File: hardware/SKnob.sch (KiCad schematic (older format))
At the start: 68 parts, among them J1 USB_B_Micro, J2 Conn_01x02, J3 Conn_01x02, SW1 SW_Push, T1 LA_LOGO, T2 LA_LOGO, U1 STM32WB55Cx, U2 LIS2DE12TR, U3 USBLC6-2P6, Y1 32MHz, Y2 32.768kHz

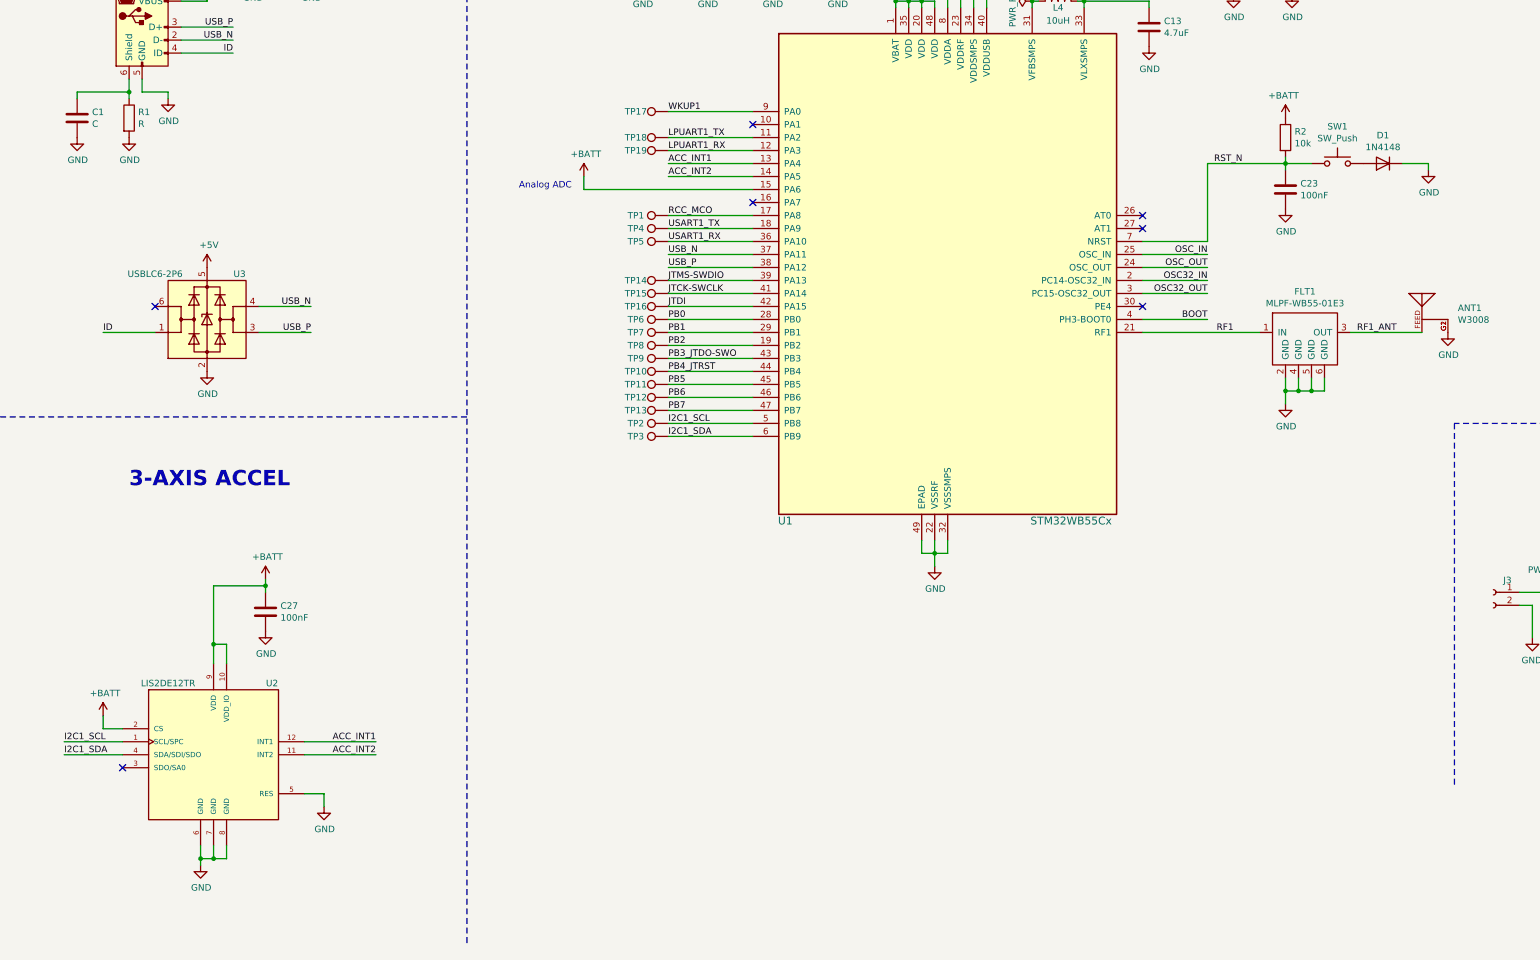
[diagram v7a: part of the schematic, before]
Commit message: added buzzer to PE4
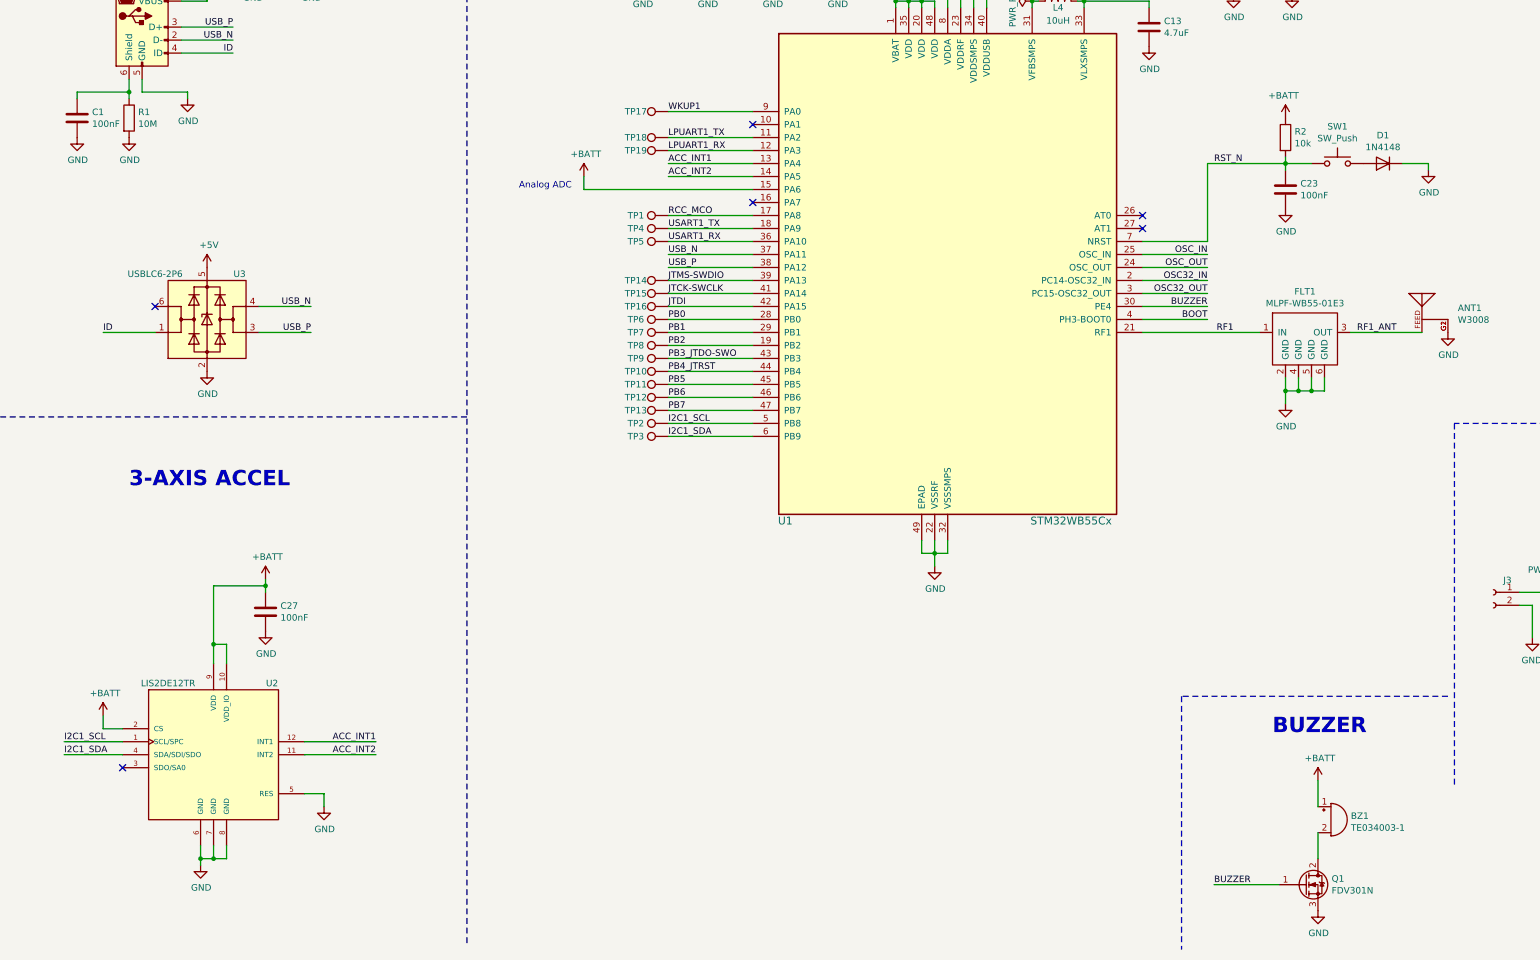
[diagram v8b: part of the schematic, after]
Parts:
- added BZ1: TE034003-1, SKnob:TE034003-1, symbol Device:Buzzer
- added Q1: FDV301N, Package_TO_SOT_SMD:SOT-23, symbol Device:Q_NMOS_GDS
- ANT1: Info 2.4GHz Bluetooth Chip RF Antenna 2.4GHz ~ 2.483GHz 1.7dBi S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 -> (none); info (none) -> 2.4GHz Bluetooth Chip RF Antenna 2.4GHz ~ 2.483GHz 1.7dBi S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
- BT1: Info Battery Retainer Coin, 12.0mm 1 Cell SMD (SMT) Tab -> (none); info (none) -> Battery Retainer Coin, 12.0mm 1 Cell SMD (SMT) Tab
- C1: value C -> 100nF
- D1: Info Diode Standard 100V 150mA Surface Mount DFN1006-2 -> (none); info (none) -> Diode Standard 100V 150mA Surface Mount DFN1006-2
- FLT1: Info 2.45GHz Center Frequency Low Pass RF Filter (Radio Frequenc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 -> (none); info (none) -> 2.45GHz Center Frequency Low Pass RF Filter (Radio Frequenc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
- L4: Info 10µH Unshielded Wirewound Inductor 380mA 468mOhm Max 0603 (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 -> (none); info (none) -> 10µH Unshielded Wirewound Inductor 380mA 468mOhm Max 0603 (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
- R1: value R -> 10M
- U1: Info IC RF TxRx + MCU 802.15.4, Bluetooth Bluetooth v5.0 2.405GH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 -> (none); info (none) -> IC RF TxRx + MCU 802.15.4, Bluetooth Bluetooth v5.0 2.405GH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
- U2: Info Accelerometer X, Y, Z Axis ±2g, 4g, 8g, 16g 0.5Hz ~ 2.69kHz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 -> (none); info (none) -> Accelerometer X, Y, Z Axis ±2g, 4g, 8g, 16g 0.5Hz ~ 2.69kHz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
- U3: Info 17V Clamp 5A (8/20µs) Ipp Tvs Diode Surface Mount SOT-666 -> (none); info (none) -> 17V Clamp 5A (8/20µs) Ipp Tvs Diode Surface Mount SOT-666
- Y1: Info 32MHz ±10ppm Crystal 10pF 60 Ohms 4-SMD, No Lead -> (none); info (none) -> 32MHz ±10ppm Crystal 10pF 60 Ohms 4-SMD, No Lead
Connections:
- net +BATT: now also BZ1.1 (-)
- net GND: now also Q1.3 (S)
- net BUZZER: now reaches U1.30 (PE4)
- net BUZZER: now also Q1.1 (G)
- new net: BZ1.2 (+), Q1.2 (D)
- no-connect marks 7 -> 6
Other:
- note added: "BUZZER"
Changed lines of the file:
@@
 F 2 "Battery:BatteryHolder_Keystone_3000_1x12mm" V 14800 8760 50  0001 C CNN
 F 3 "https://www.memoryprotectiondevices.com/datasheets/BK-885-datasheet.pdf" V 14800 8760 50  0001 C CNN
-F 4 "Battery Retainer Coin, 12.0mm 1 Cell SMD (SMT) Tab" H 14918 8659 50  0001 L CNN "Info"
-F 5 "MPD (Memory Protection Devices)" H 14800 8700 50  0001 C CNN "manf"
-F 6 "BK-885-TR" H 14800 8700 50  0001 C CNN "manf#"
-F 7 "BK-885-CT-ND" H 14800 8700 50  0001 C CNN "digikey#"
+F 4 "MPD (Memory Protection Devices)" H 14800 8700 50  0001 C CNN "manf"
+F 5 "BK-885-TR" H 14800 8700 50  0001 C CNN "manf#"
+F 6 "BK-885-CT-ND" H 14800 8700 50  0001 C CNN "digikey#"
+F 7 "Battery Retainer Coin, 12.0mm 1 Cell SMD (SMT) Tab" H 14800 8700 50  0001 C CNN "info"
 	1    14800 8700
 	1    0    0    -1
@@
 F 5 "W3008" H 11550 6350 50  0001 C CNN "manf#"
 F 6 "PulseLarsen Antennas" H 11550 6350 50  0001 C CNN "manf"
-F 7 "2.4GHz Bluetooth Chip RF Antenna 2.4GHz ~ 2.483GHz 1.7dBi Solder Surface Mount" H 11550 6350 50  0001 C CNN "Info"
+F 7 "2.4GHz Bluetooth Chip RF Antenna 2.4GHz ~ 2.483GHz 1.7dBi Solder Surface Mount" H 11550 6350 50  0001 C CNN "info"
 	1    11550 6350
 	1    0    0    -1
@@
 F 5 "STMicroelectronics" H 6400 4750 50  0001 C CNN "manf"
 F 6 "STM32WB55CGU6" H 6400 4750 50  0001 C CNN "manf#"
-F 7 "IC RF TxRx + MCU 802.15.4, Bluetooth Bluetooth v5.0 2.405GHz ~ 2.48GHz 48-UFQFN Exposed Pad" H 6400 4750 50  0001 C CNN "Info"
+F 7 "IC RF TxRx + MCU 802.15.4, Bluetooth Bluetooth v5.0 2.405GHz ~ 2.48GHz 48-UFQFN Exposed Pad" H 6400 4750 50  0001 C CNN "info"
 	1    6400 4750
 	1    0    0    -1
@@
 F 5 "CBMF1608T100K" V 8750 3900 50  0001 C CNN "manf#"
 F 6 "587-1720-1-ND" V 8750 3900 50  0001 C CNN "digikey#"
-F 7 "10µH Unshielded Wirewound Inductor 380mA 468mOhm Max 0603 (1608 Metric)" H 8750 3900 50  0001 C CNN "Info"
+F 7 "10µH Unshielded Wirewound Inductor 380mA 468mOhm Max 0603 (1608 Metric)" H 8750 3900 50  0001 C CNN "info"
 	1    8750 3900
 	0    -1   -1   0
@@
 P 1600 4800
 F 0 "R1" H 1670 4846 50  0000 L CNN
-F 1 "R" H 1670 4755 50  0000 L CNN
+F 1 "10M" H 1670 4755 50  0000 L CNN
 F 2 "Resistor_SMD:R_0402_1005Metric" V 1530 4800 50  0001 C CNN
 F 3 "~" H 1600 4800 50  0001 C CNN
@@
 P 1200 4800
 F 0 "C1" H 1315 4846 50  0000 L CNN
-F 1 "C" H 1315 4755 50  0000 L CNN
+F 1 "100nF" H 1315 4755 50  0000 L CNN
 F 2 "Capacitor_SMD:C_0402_1005Metric" H 1238 4650 50  0001 C CNN
 F 3 "~" H 1200 4800 50  0001 C CNN
@@
 L power:GND #PWR?
 U 1 1 5EE31E11
-P 1900 4650
-F 0 "#PWR?" H 1900 4400 50  0001 C CNN
-F 1 "GND" H 1905 4477 50  0000 C CNN
-F 2 "" H 1900 4650 50  0001 C CNN
-F 3 "" H 1900 4650 50  0001 C CNN
-	1    1900 4650
-	1    0    0    -1
-$EndComp
-Wire Wire Line
-	1900 4600 1700 4600
+P 2050 4650
+F 0 "#PWR?" H 2050 4400 50  0001 C CNN
+F 1 "GND" H 2055 4477 50  0000 C CNN
+F 2 "" H 2050 4650 50  0001 C CNN
+F 3 "" H 2050 4650 50  0001 C CNN
+	1    2050 4650
+	1    0    0    -1
+$EndComp
+Wire Wire Line
+	2050 4600 1700 4600
 Wire Wire Line
 	1700 4600 1700 4500
 Wire Wire Line
-	1900 4600 1900 4650
+	2050 4600 2050 4650
 Wire Wire Line
 	2400 4300 2000 4300
@@
 F 2 "Crystal:Crystal_SMD_2016-4Pin_2.0x1.6mm" H 14450 4550 50  0001 C CNN
 F 3 "https://www.murata.com/products/productdata/8801065041950/SPEC-XRCGB32M000F1H02R0.pdf" H 14450 4550 50  0001 C CNN
-F 4 "32MHz ±10ppm Crystal 10pF 60 Ohms 4-SMD, No Lead" H 14450 4550 50  0001 C CNN "Info"
-F 5 "490-18335-1-ND" H 14450 4550 50  0001 C CNN "digikey#"
-F 6 "Murata Electronics" H 14450 4550 50  0001 C CNN "manf"
-F 7 "XRCGB32M000F1H02R0" H 14450 4550 50  0001 C CNN "manf#"
+F 4 "490-18335-1-ND" H 14450 4550 50  0001 C CNN "digikey#"
+F 5 "Murata Electronics" H 14450 4550 50  0001 C CNN "manf"
+F 6 "XRCGB32M000F1H02R0" H 14450 4550 50  0001 C CNN "manf#"
+F 7 "32MHz ±10ppm Crystal 10pF 60 Ohms 4-SMD, No Lead" H 14450 4550 50  0001 C CNN "info"
 	1    14450 4550
 	1    0    0    -1
@@
 F 2 "Crystal:Crystal_SMD_2016-4Pin_2.0x1.6mm" H 14450 6200 50  0001 C CNN
 F 3 "~" H 14450 6200 50  0001 C CNN
+F 4 "" H 14450 6200 50  0001 C CNN "info"
 	1    14450 6200
 	1    0    0    -1
@@
 F 5 "1N4148WL2-TP" H 11250 5150 50  0001 C CNN "manf#"
 F 6 "1N4148WL2-TPMSCT-ND" H 11250 5150 50  0001 C CNN "digikey#"
-F 7 "Diode Standard 100V 150mA Surface Mount DFN1006-2" H 11250 5150 50  0001 C CNN "Info"
+F 7 "Diode Standard 100V 150mA Surface Mount DFN1006-2" H 11250 5150 50  0001 C CNN "info"
 	1    11250 5150
 	-1   0    0    1
@@
 Text Label 2400 4300 2    50   ~ 0
 ID
-NoConn ~ 9400 6250
 Wire Wire Line
 	3000 3350 3150 3350
@@
 F 5 "STMicroelectronics" H 2250 9700 50  0001 L BNN "manf"
 F 6 "497-15997-1-ND " H 2250 9700 50  0001 C CNN "digikey#"
-F 7 "Accelerometer X, Y, Z Axis ±2g, 4g, 8g, 16g 0.5Hz ~ 2.69kHz 12-LGA (2x2)" H 2250 9700 50  0001 C CNN "Info"
+F 7 "Accelerometer X, Y, Z Axis ±2g, 4g, 8g, 16g 0.5Hz ~ 2.69kHz 12-LGA (2x2)" H 2250 9700 50  0001 C CNN "info"
 	1    2250 9700
 	1    0    0    -1
@@
 F 2 "Package_TO_SOT_SMD:SOT-666" H 2200 5850 50  0001 C CNN
 F 3 "https://www.st.com/resource/en/datasheet/usblc6-2.pdf" H 2400 6700 50  0001 C CNN
-F 4 "17V Clamp 5A (8/20µs) Ipp Tvs Diode Surface Mount SOT-666" H 2200 6350 50  0001 C CNN "Info"
-F 5 "497-5026-1-ND" H 2200 6350 50  0001 C CNN "digikey#"
-F 6 "STMicroelectronics" H 2200 6350 50  0001 C CNN "manf"
-F 7 "USBLC6-2P6" H 2200 6350 50  0001 C CNN "manf#"
+F 4 "497-5026-1-ND" H 2200 6350 50  0001 C CNN "digikey#"
+F 5 "STMicroelectronics" H 2200 6350 50  0001 C CNN "manf"
+F 6 "USBLC6-2P6" H 2200 6350 50  0001 C CNN "manf#"
+F 7 "17V Clamp 5A (8/20µs) Ipp Tvs Diode Surface Mount SOT-666" H 2200 6350 50  0001 C CNN "info"
 	1    2200 6350
 	1    0    0    -1
@@
 F 5 "STMicroelectronics" H 10650 6450 50  0001 C CNN "manf"
 F 6 "MLPF-WB55-01E3" H 10650 6450 50  0001 C CNN "manf#"
-F 7 "2.45GHz Center Frequency Low Pass RF Filter (Radio Frequency) 100MHz Bandwidth 1.1dB 6-SMD, No Lead" H 10650 6450 50  0001 C CNN "Info"
+F 7 "2.45GHz Center Frequency Low Pass RF Filter (Radio Frequency) 100MHz Bandwidth 1.1dB 6-SMD, No Lead" H 10650 6450 50  0001 C CNN "info"
 	1    10650 6450
 	1    0    0    -1
@@
 F 5 "BR-1225" H 15700 8150 50  0001 C CNN "manf#"
 F 6 "P183-ND" H 15700 8050 50  0001 C CNN "digikey#"
-F 7 "Coin, 12.5mm Lithium Poly-Carbon Monoflouride 3V Battery Non-Rechargeable (Primary)" H 15700 7950 50  0001 C CNN "info"
+F 7 "Coin, 12.5mm Lithium Poly-Carbon Monoflouride 3V Battery Non-Rechargeable (Primary)" H 15700 8700 50  0001 C CNN "info"
 	1    15700 8700
 	1    0    0    -1
@@
 	0    -1   -1   0
 $EndComp
+$Comp
+L Device:Buzzer BZ1
+U 1 1 5F285DB8
+P 10850 10200
+F 0 "BZ1" H 11003 10229 50  0000 L CNN
+F 1 "TE034003-1" H 11003 10138 50  0000 L CNN
+F 2 "SKnob:TE034003-1" V 10825 10300 50  0001 C CNN
+F 3 "https://dbunlimitedco.com/images/product_images/2D-Drawings/TE034003-1.pdf" V 10825 10300 50  0001 C CNN
+F 4 "DB Unlimited" H 10850 10200 50  0001 C CNN "manf"
+F 5 "TE034003-1" H 10850 10200 50  0001 C CNN "manf#"
+F 6 "2104-TE034003-1CT-ND" H 10850 10200 50  0001 C CNN "digikey#"
+	1    10850 10200
+	1    0    0    -1
+$EndComp
+$Comp
+L power:GND #PWR?
+U 1 1 5F2A26BC
+P 10750 10900
+F 0 "#PWR?" H 10750 10650 50  0001 C CNN
+F 1 "GND" H 10755 10727 50  0000 C CNN
+F 2 "" H 10750 10900 50  0001 C CNN
+F 3 "" H 10750 10900 50  0001 C CNN
+	1    10750 10900
+	1    0    0    -1
+$EndComp
+$Comp
+L Device:Q_NMOS_GDS Q1
+U 1 1 5F2B0049
+P 10650 10700
+F 0 "Q1" H 10855 10746 50  0000 L CNN
+F 1 "FDV301N" H 10855 10655 50  0000 L CNN
+F 2 "Package_TO_SOT_SMD:SOT-23" H 10850 10800 50  0001 C CNN
+F 3 "https://media.digikey.com/pdf/Data%20Sheets/Fairchild%20PDFs/FDV301N.pdf" H 10650 10700 50  0001 C CNN
+F 4 "ON Semiconductor" H 10650 10700 50  0001 C CNN "manf"
+F 5 "FDV301N" H 10650 10700 50  0001 C CNN "manf#"
+F 6 "FDV301NCT-ND" H 10650 10700 50  0001 C CNN "digikey#"
+	1    10650 10700
+	1    0    0    -1
+$EndComp
+Wire Wire Line
+	10750 10300 10750 10500
+Wire Wire Line
+	10750 10100 10750 9900
+$Comp
+L power:+BATT #PWR?
+U 1 1 5F2E4EB0
+P 10750 9900
+F 0 "#PWR?" H 10750 9750 50  0001 C CNN
+F 1 "+BATT" H 10765 10073 50  0000 C CNN
+F 2 "" H 10750 9900 50  0001 C CNN
+F 3 "" H 10750 9900 50  0001 C CNN
+	1    10750 9900
+	1    0    0    -1
+$EndComp
+Wire Wire Line
+	9400 6250 9900 6250
+Text Label 9900 6250 2    50   ~ 0
+BUZZER
+Wire Wire Line
+	10450 10700 9950 10700
+Text Label 9950 10700 0    50   ~ 0
+BUZZER
+Wire Notes Line
+	11750 9250 9700 9250
+Wire Notes Line
+	9700 9250 9700 11200
+Text Notes 10400 9550 0    118  ~ 24
+BUZZER
 $EndSCHEMATC
